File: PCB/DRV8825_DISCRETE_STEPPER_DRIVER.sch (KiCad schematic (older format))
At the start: 10 parts

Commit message: Added 12V regulator
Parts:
- C? (x3): Voltage Rating (none) -> 50V
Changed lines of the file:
@@
 $Descr A4 11693 8268
 encoding utf-8
-Sheet 4 19
+Sheet 4 20
 Title ""
 Date ""
@@
 U 1 1 5E8D91C5
 P 4500 4550
+AR Path="/5E8A6686/5E8D27A6/5E8D91C5" Ref="#PWR?"  Part="1"
+AR Path="/5E8813FF/5E8D27A6/5E8D91C5" Ref="#PWR?"  Part="1"
 F 0 "#PWR?" H 4500 4300 50  0001 C CNN
 F 1 "GND" V 4505 4422 50  0000 R CNN
@@
 U 1 1 5E8D92EE
 P 4500 4650
+AR Path="/5E8A6686/5E8D27A6/5E8D92EE" Ref="#PWR?"  Part="1"
+AR Path="/5E8813FF/5E8D27A6/5E8D92EE" Ref="#PWR?"  Part="1"
 F 0 "#PWR?" H 4500 4400 50  0001 C CNN
 F 1 "GND" V 4505 4522 50  0000 R CNN
@@
 U 1 1 5E8DCE8F
 P 5100 4050
+AR Path="/5E8A6686/5E8D27A6/5E8DCE8F" Ref="#PWR?"  Part="1"
+AR Path="/5E8813FF/5E8D27A6/5E8DCE8F" Ref="#PWR?"  Part="1"
 F 0 "#PWR?" H 5100 3800 50  0001 C CNN
 F 1 "GND" V 5105 3922 50  0000 R CNN
@@
 U 1 1 5E8DD0CD
 P 5100 3950
+AR Path="/5E8A6686/5E8D27A6/5E8DD0CD" Ref="#PWR?"  Part="1"
+AR Path="/5E8813FF/5E8D27A6/5E8DD0CD" Ref="#PWR?"  Part="1"
 F 0 "#PWR?" H 5100 3700 50  0001 C CNN
 F 1 "GND" V 5105 3822 50  0000 R CNN
@@
 U 1 1 5E8DD1EC
 P 5100 3850
+AR Path="/5E8A6686/5E8D27A6/5E8DD1EC" Ref="#PWR?"  Part="1"
+AR Path="/5E8813FF/5E8D27A6/5E8DD1EC" Ref="#PWR?"  Part="1"
 F 0 "#PWR?" H 5100 3600 50  0001 C CNN
 F 1 "GND" V 5105 3722 50  0000 R CNN
@@
 U 1 1 5E8E02D7
 P 4600 3650
+AR Path="/5E8A6686/5E8D27A6/5E8E02D7" Ref="#PWR?"  Part="1"
+AR Path="/5E8813FF/5E8D27A6/5E8E02D7" Ref="#PWR?"  Part="1"
 F 0 "#PWR?" H 4600 3400 50  0001 C CNN
 F 1 "GND" H 4605 3477 50  0000 C CNN
@@
 U 1 1 5E8E181B
 P 6500 3700
+AR Path="/5E8A6686/5E8D27A6/5E8E181B" Ref="C?"  Part="1"
+AR Path="/5E8813FF/5E8D27A6/5E8E181B" Ref="C?"  Part="1"
 F 0 "C?" H 6592 3746 50  0000 L CNN
 F 1 "470nF" H 6592 3655 50  0000 L CNN
@@
 U 1 1 5E8E24E3
 P 6500 3850
+AR Path="/5E8A6686/5E8D27A6/5E8E24E3" Ref="#PWR?"  Part="1"
+AR Path="/5E8813FF/5E8D27A6/5E8E24E3" Ref="#PWR?"  Part="1"
 F 0 "#PWR?" H 6500 3600 50  0001 C CNN
 F 1 "GND" H 6505 3677 50  0000 C CNN
@@
 U 1 1 5E8E69E3
 P 5650 5100
+AR Path="/5E8A6686/5E8D27A6/5E8E69E3" Ref="#PWR?"  Part="1"
+AR Path="/5E8813FF/5E8D27A6/5E8E69E3" Ref="#PWR?"  Part="1"
 F 0 "#PWR?" H 5650 4850 50  0001 C CNN
 F 1 "GND" H 5655 4927 50  0000 C CNN
@@
 U 1 1 5E8E6E0E
 P 5750 5100
+AR Path="/5E8A6686/5E8D27A6/5E8E6E0E" Ref="#PWR?"  Part="1"
+AR Path="/5E8813FF/5E8D27A6/5E8E6E0E" Ref="#PWR?"  Part="1"
 F 0 "#PWR?" H 5750 4850 50  0001 C CNN
 F 1 "GND" H 5755 4927 50  0000 C CNN
@@
 U 1 1 5E8E6F63
 P 5850 5100
+AR Path="/5E8A6686/5E8D27A6/5E8E6F63" Ref="#PWR?"  Part="1"
+AR Path="/5E8813FF/5E8D27A6/5E8E6F63" Ref="#PWR?"  Part="1"
 F 0 "#PWR?" H 5850 4850 50  0001 C CNN
 F 1 "GND" H 5855 4927 50  0000 C CNN
@@
 U 1 1 5E8E9760
 P 5300 2350
+AR Path="/5E8A6686/5E8D27A6/5E8E9760" Ref="C?"  Part="1"
+AR Path="/5E8813FF/5E8D27A6/5E8E9760" Ref="C?"  Part="1"
 F 0 "C?" H 5391 2304 50  0000 L CNN
 F 1 "4.7uF" H 5391 2395 50  0000 L CNN
 F 2 "" H 5300 2350 50  0001 C CNN
 F 3 "~" H 5300 2350 50  0001 C CNN
+F 4 "50V" H 5300 2350 50  0001 C CNN "Voltage Rating"
 	1    5300 2350
 	-1   0    0    1
@@
 U 1 1 5E8E999E
 P 5700 2350
+AR Path="/5E8A6686/5E8D27A6/5E8E999E" Ref="C?"  Part="1"
+AR Path="/5E8813FF/5E8D27A6/5E8E999E" Ref="C?"  Part="1"
 F 0 "C?" H 5791 2304 50  0000 L CNN
 F 1 "100nF" H 5791 2395 50  0000 L CNN
 F 2 "" H 5700 2350 50  0001 C CNN
 F 3 "~" H 5700 2350 50  0001 C CNN
+F 4 "50V" H 5700 2350 50  0001 C CNN "Voltage Rating"
 	1    5700 2350
 	-1   0    0    1
@@
 U 1 1 5E8E9DB5
 P 6050 2350
+AR Path="/5E8A6686/5E8D27A6/5E8E9DB5" Ref="C?"  Part="1"
+AR Path="/5E8813FF/5E8D27A6/5E8E9DB5" Ref="C?"  Part="1"
 F 0 "C?" H 5958 2304 50  0000 R CNN
 F 1 "10nF" H 5958 2395 50  0000 R CNN
 F 2 "" H 6050 2350 50  0001 C CNN
 F 3 "~" H 6050 2350 50  0001 C CNN
+F 4 "50V" H 6050 2350 50  0001 C CNN "Voltage Rating"
 	1    6050 2350
 	-1   0    0    1
@@
 U 1 1 5E8F0245
 P 5300 2500
+AR Path="/5E8A6686/5E8D27A6/5E8F0245" Ref="#PWR?"  Part="1"
+AR Path="/5E8813FF/5E8D27A6/5E8F0245" Ref="#PWR?"  Part="1"
 F 0 "#PWR?" H 5300 2250 50  0001 C CNN
 F 1 "GND" H 5305 2327 50  0000 C CNN
@@
 U 1 1 5E8F04AF
 P 5700 2500
+AR Path="/5E8A6686/5E8D27A6/5E8F04AF" Ref="#PWR?"  Part="1"
+AR Path="/5E8813FF/5E8D27A6/5E8F04AF" Ref="#PWR?"  Part="1"
 F 0 "#PWR?" H 5700 2250 50  0001 C CNN
 F 1 "GND" H 5705 2327 50  0000 C CNN
@@
 U 1 1 5E8F06A3
 P 6050 2500
+AR Path="/5E8A6686/5E8D27A6/5E8F06A3" Ref="#PWR?"  Part="1"
+AR Path="/5E8813FF/5E8D27A6/5E8F06A3" Ref="#PWR?"  Part="1"
 F 0 "#PWR?" H 6050 2250 50  0001 C CNN
 F 1 "GND" H 6055 2327 50  0000 C CNN

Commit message: Cleanup
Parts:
- U?: DK_Datasheet_Link http://www.ti.com/general/docs/suppproductinfo.tsp?distId=1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 -> (none); DK_Detail_Page /product-detail/en/texas-instruments/DRV8825PWPR/296-29503-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 -> (none)
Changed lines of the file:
@@
 F 6 "Integrated Circuits (ICs)" H 5750 4450 60  0001 L CNN "Category"
 F 7 "PMIC - Motor Drivers, Controllers" H 5750 4550 60  0001 L CNN "Family"
-F 8 "http://www.ti.com/general/docs/suppproductinfo.tsp?distId=10&gotoUrl=http%3A%2F%2Fwww.ti.com%2Flit%2Fgpn%2Fdrv8825" H 5750 4650 60  0001 L CNN "DK_Datasheet_Link"
-F 9 "/product-detail/en/texas-instruments/DRV8825PWPR/296-29503-1-ND/2749200" H 5750 4750 60  0001 L CNN "DK_Detail_Page"
+F 8 "" H 5750 4650 60  0001 L CNN "DK_Datasheet_Link"
+F 9 "" H 5750 4750 60  0001 L CNN "DK_Detail_Page"
 F 10 "IC MTR DRVR BIPLR 8.2-45V 28SSOP" H 5750 4850 60  0001 L CNN "Description"
 F 11 "Texas Instruments" H 5750 4950 60  0001 L CNN "Manufacturer"

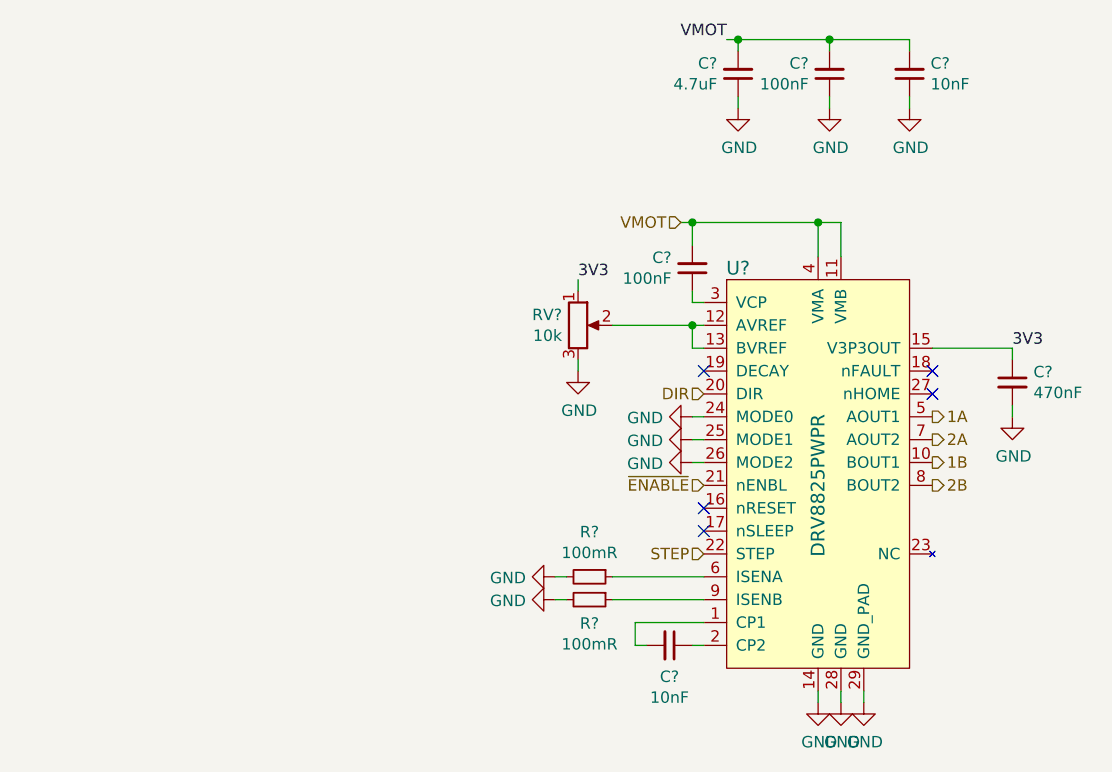
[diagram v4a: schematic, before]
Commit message: Added resistors to set stepper motor current
Once a current is specified the pot can be removed in favor of resistors for production ease
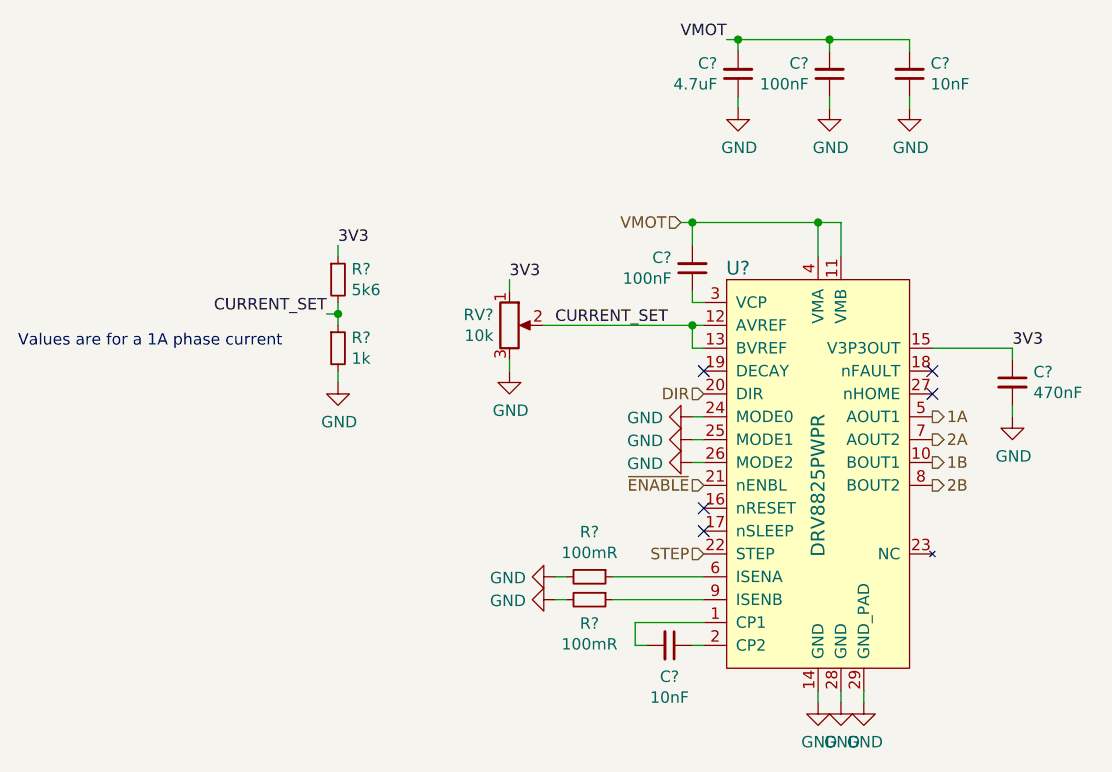
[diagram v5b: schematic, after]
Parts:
- added R?: 5k6, symbol Device:R_Small
- added R?: 1k, symbol Device:R_Small
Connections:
- net 3V3: now also R?.1
- net GND: now also R?.2
- net CURRENT_SET: now reaches RV?.2, U?.12 (AVREF), U?.13 (BVREF)
- net CURRENT_SET: now also R?.1, R?.2
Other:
- note added: "Values are for a 1A phase current"
- moved on the sheet: RV?
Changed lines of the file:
@@
 $Descr A4 11693 8268
 encoding utf-8
-Sheet 12 20
+Sheet 4 20
 Title ""
 Date ""
@@
 L Device:R_POT RV?
 U 1 1 5E8DF1FC
-P 4600 3450
+P 4300 3450
 AR Path="/5E8A6686/5E8D27A6/5E8DF1FC" Ref="RV?"  Part="1"
 AR Path="/5E8813FF/5E8D27A6/5E8DF1FC" Ref="RV?"  Part="1"
-F 0 "RV?" H 4530 3496 50  0000 R CNN
-F 1 "10k" H 4530 3405 50  0000 R CNN
-F 2 "" H 4600 3450 50  0001 C CNN
-F 3 "~" H 4600 3450 50  0001 C CNN
-	1    4600 3450
-	1    0    0    -1
-$EndComp
-Wire Wire Line
-	4600 3250 4600 3300
+F 0 "RV?" H 4230 3496 50  0000 R CNN
+F 1 "10k" H 4230 3405 50  0000 R CNN
+F 2 "" H 4300 3450 50  0001 C CNN
+F 3 "~" H 4300 3450 50  0001 C CNN
+	1    4300 3450
+	1    0    0    -1
+$EndComp
+Wire Wire Line
+	4300 3250 4300 3300
 $Comp
 L power:GND #PWR?
 U 1 1 5E8E02D7
-P 4600 3650
+P 4300 3650
 AR Path="/5E8A6686/5E8D27A6/5E8E02D7" Ref="#PWR?"  Part="1"
 AR Path="/5E8813FF/5E8D27A6/5E8E02D7" Ref="#PWR?"  Part="1"
-F 0 "#PWR?" H 4600 3400 50  0001 C CNN
-F 1 "GND" H 4605 3477 50  0000 C CNN
-F 2 "" H 4600 3650 50  0001 C CNN
-F 3 "" H 4600 3650 50  0001 C CNN
-	1    4600 3650
-	1    0    0    -1
-$EndComp
-Wire Wire Line
-	4600 3600 4600 3650
-Wire Wire Line
-	4750 3450 5100 3450
+F 0 "#PWR?" H 4300 3400 50  0001 C CNN
+F 1 "GND" H 4305 3477 50  0000 C CNN
+F 2 "" H 4300 3650 50  0001 C CNN
+F 3 "" H 4300 3650 50  0001 C CNN
+	1    4300 3650
+	1    0    0    -1
+$EndComp
+Wire Wire Line
+	4300 3600 4300 3650
+Wire Wire Line
+	4450 3450 5100 3450
 Wire Wire Line
 	5150 3550 5100 3550
@@
 Wire Wire Line
 	5300 2500 5300 2450
-Text Label 4600 3250 0    50   ~ 0
+Text Label 4300 3250 0    50   ~ 0
 3V3
 Text Label 6500 3550 0    50   ~ 0
 3V3
+Text Label 4500 3450 0    50   ~ 0
+CURRENT_SET
+$Comp
+L Device:R_Small R?
+U 1 1 5E8B797B
+P 3550 3250
+F 0 "R?" H 3609 3296 50  0000 L CNN
+F 1 "5k6" H 3609 3205 50  0000 L CNN
+F 2 "" H 3550 3250 50  0001 C CNN
+F 3 "~" H 3550 3250 50  0001 C CNN
+	1    3550 3250
+	1    0    0    -1
+$EndComp
+$Comp
+L Device:R_Small R?
+U 1 1 5E8B7AF6
+P 3550 3550
+F 0 "R?" H 3609 3596 50  0000 L CNN
+F 1 "1k" H 3609 3505 50  0000 L CNN
+F 2 "" H 3550 3550 50  0001 C CNN
+F 3 "~" H 3550 3550 50  0001 C CNN
+	1    3550 3550
+	1    0    0    -1
+$EndComp
+$Comp
+L power:GND #PWR?
+U 1 1 5E8B7CD9
+P 3550 3700
+AR Path="/5E8A6686/5E8D27A6/5E8B7CD9" Ref="#PWR?"  Part="1"
+AR Path="/5E8813FF/5E8D27A6/5E8B7CD9" Ref="#PWR?"  Part="1"
+F 0 "#PWR?" H 3550 3450 50  0001 C CNN
+F 1 "GND" H 3555 3527 50  0000 C CNN
+F 2 "" H 3550 3700 50  0001 C CNN
+F 3 "" H 3550 3700 50  0001 C CNN
+	1    3550 3700
+	1    0    0    -1
+$EndComp
+Wire Wire Line
+	3550 3650 3550 3700
+Text Label 3500 3400 2    50   ~ 0
+CURRENT_SET
+Wire Wire Line
+	3500 3400 3550 3400
+Wire Wire Line
+	3550 3400 3550 3350
+Wire Wire Line
+	3550 3450 3550 3400
+Connection ~ 3550 3400
+Text Label 3550 3100 0    50   ~ 0
+3V3
+Wire Wire Line
+	3550 3100 3550 3150
+Text Notes 2150 3550 0    50   ~ 0
+Values are for a 1A phase current
 $EndSCHEMATC

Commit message: Removed DK additional fields
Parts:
- U?: Category Integrated Circuits (ICs) -> (none); Description IC MTR DRVR BIPLR 8.2-45V 28SSOP -> (none); Digi-Key_PN 296-29503-1-ND -> (none); Family PMIC - Motor Drivers, Controllers -> (none); Status Active -> (none)
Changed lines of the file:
@@
 F 2 "digikey-footprints:TSSOP-28-1EP_W4.40mm" H 5750 4050 60  0001 L CNN
 F 3 "http://www.ti.com/general/docs/suppproductinfo.tsp?distId=10&gotoUrl=http%3A%2F%2Fwww.ti.com%2Flit%2Fgpn%2Fdrv8825" H 5750 4150 60  0001 L CNN
-F 4 "296-29503-1-ND" H 5750 4250 60  0001 L CNN "Digi-Key_PN"
-F 5 "DRV8825PWPR" H 5750 4350 60  0001 L CNN "MPN"
-F 6 "Integrated Circuits (ICs)" H 5750 4450 60  0001 L CNN "Category"
-F 7 "PMIC - Motor Drivers, Controllers" H 5750 4550 60  0001 L CNN "Family"
-F 8 "" H 5750 4650 60  0001 L CNN "DK_Datasheet_Link"
-F 9 "" H 5750 4750 60  0001 L CNN "DK_Detail_Page"
-F 10 "IC MTR DRVR BIPLR 8.2-45V 28SSOP" H 5750 4850 60  0001 L CNN "Description"
-F 11 "Texas Instruments" H 5750 4950 60  0001 L CNN "Manufacturer"
-F 12 "Active" H 5750 5050 60  0001 L CNN "Status"
+F 4 "DRV8825PWPR" H 5750 4350 60  0001 L CNN "MPN"
+F 5 "Texas Instruments" H 5750 4950 60  0001 L CNN "Manufacturer"
 	1    5550 3850
 	1    0    0    -1
@@
 U 1 1 5E8B797B
 P 3550 3250
+AR Path="/5E8A6686/5E8D27A6/5E8B797B" Ref="R?"  Part="1"
+AR Path="/5E8813FF/5E8D27A6/5E8B797B" Ref="R?"  Part="1"
 F 0 "R?" H 3609 3296 50  0000 L CNN
 F 1 "5k6" H 3609 3205 50  0000 L CNN
@@
 U 1 1 5E8B7AF6
 P 3550 3550
+AR Path="/5E8A6686/5E8D27A6/5E8B7AF6" Ref="R?"  Part="1"
+AR Path="/5E8813FF/5E8D27A6/5E8B7AF6" Ref="R?"  Part="1"
 F 0 "R?" H 3609 3596 50  0000 L CNN
 F 1 "1k" H 3609 3505 50  0000 L CNN

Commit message: Annotated Schematic
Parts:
- gave numbers to parts that had none: 12
